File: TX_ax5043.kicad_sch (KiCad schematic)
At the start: 32 parts, among them P101 U_FL, U156 AX5043, U89 TPS22917DBV

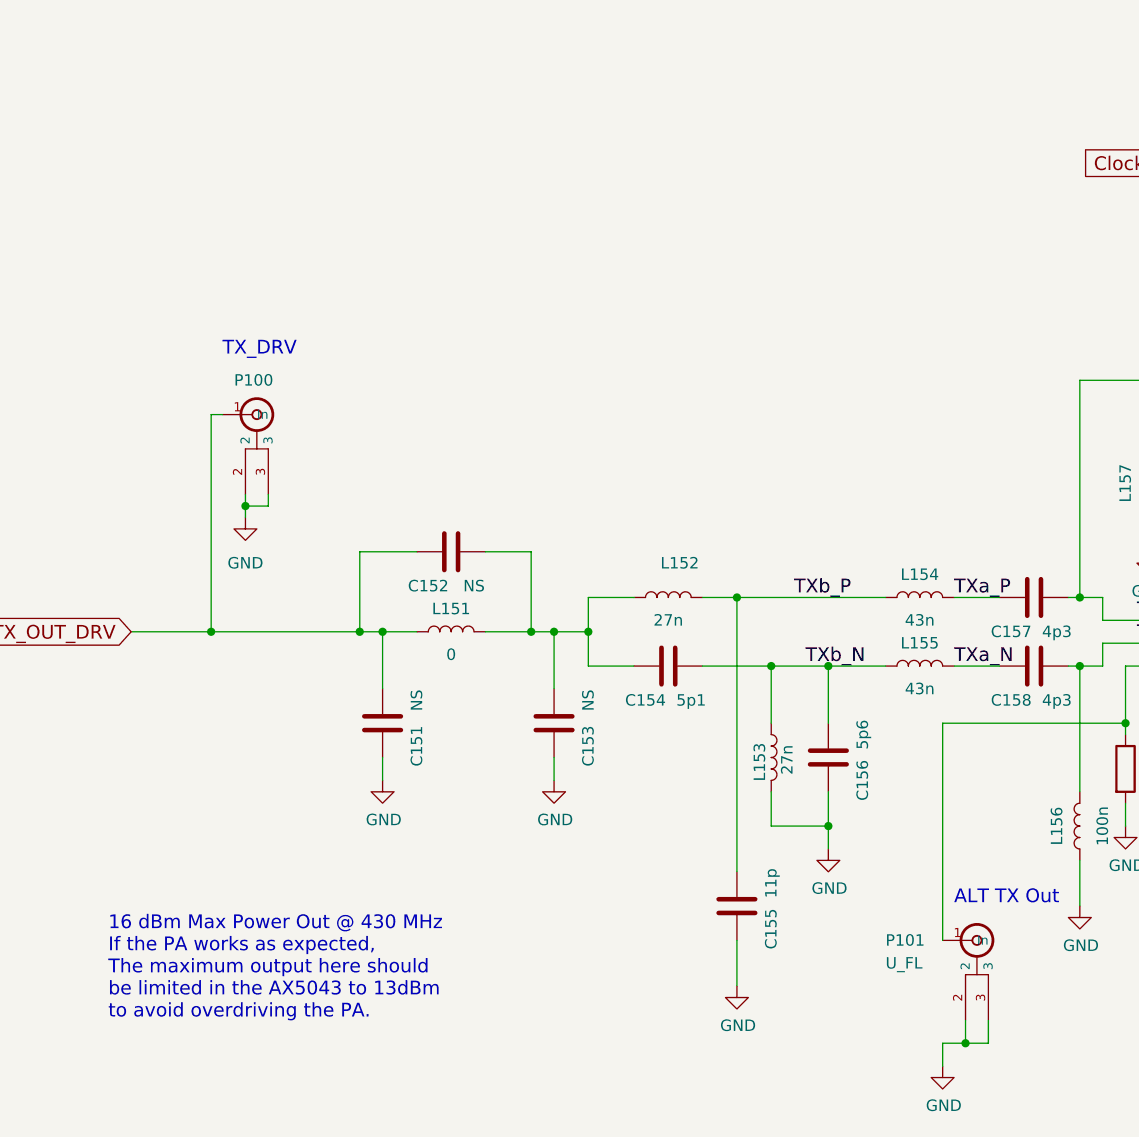
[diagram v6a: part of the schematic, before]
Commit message: Add shields around AX5043s, replace UFL connectors
Signed-off-by: Corey Minyard <corey@minyard.net>
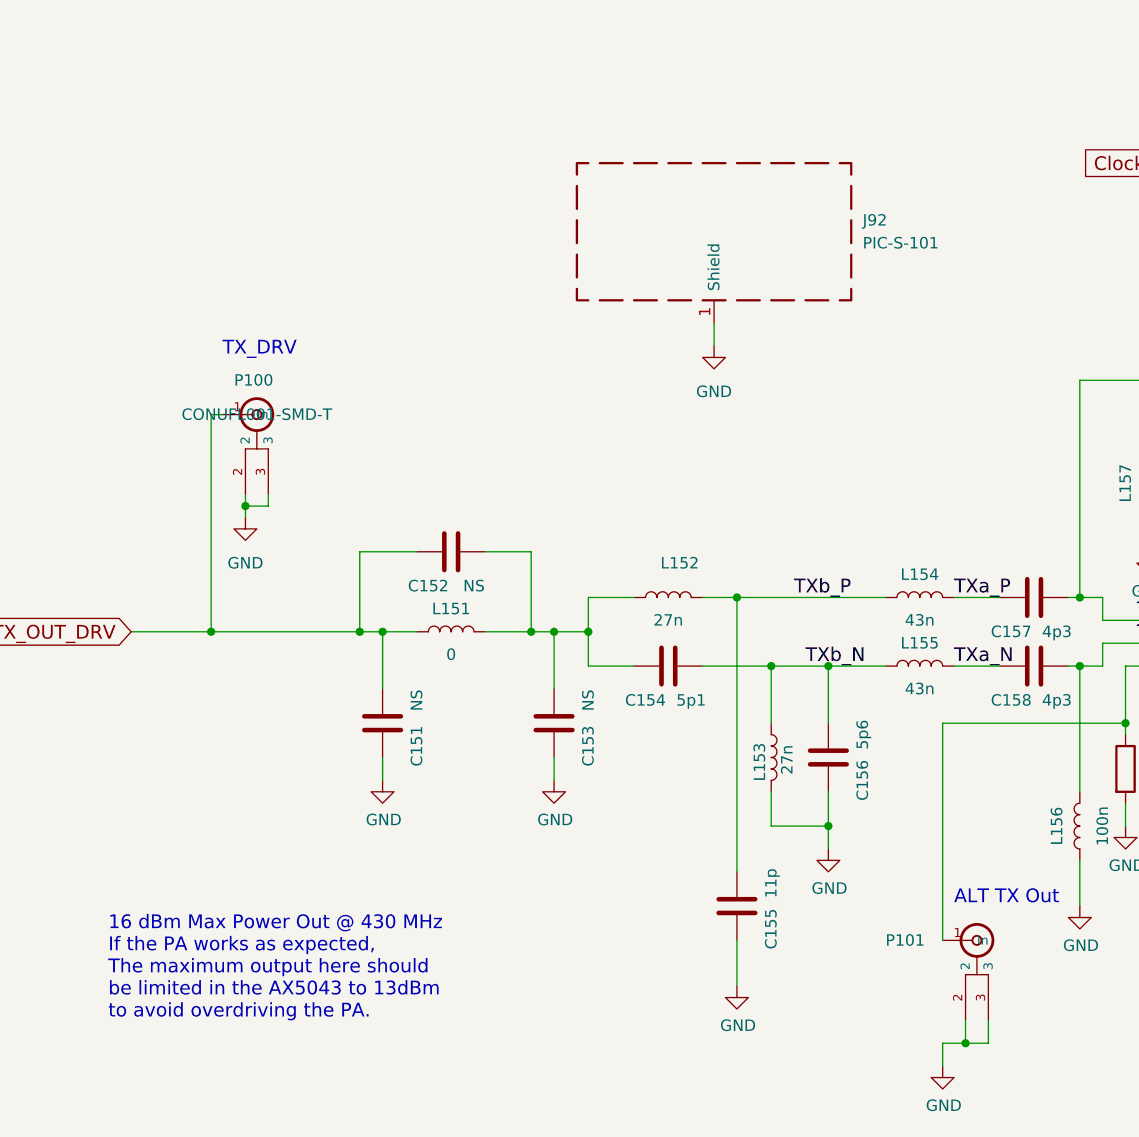
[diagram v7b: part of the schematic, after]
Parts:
- added J92: PIC-S-101, PacSatDev_misc:RF_SHIELD_PIC_S_101, symbol Device:RFShield_OnePiece
- P100: value ~ -> CONUFL001-SMD-T; footprint PacSatDev_misc:U_FL -> PacSatDev_misc:CONN1_CONUFL_TEC
- P101: value U_FL -> CONUFL001-SMD-T; footprint PacSatDev_misc:U_FL -> PacSatDev_misc:CONN1_CONUFL_TEC
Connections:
- net GND: now also J92.1 (Shield)
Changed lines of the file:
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@@
 	(wire
 		(pts
+			(xy 177.8 101.6) (xy 177.8 104.14)
+		)
+		(stroke
+			(width 0)
+			(type default)
+		)
+	)
+	(wire
+		(pts
 			(xy 256.54 176.53) (xy 262.89 176.53)
 		)
@@
 	)
 	(symbol
+		(lib_id "power:GND")
+		(at 177.8 104.14 0)
+		(unit 1)
+		(exclude_from_sim no)
+		(in_bom yes)
+		(on_board yes)
+		(dnp no)
+		(fields_autoplaced yes)
+		(property "Reference" "#PWR0208"
+			(at 177.8 110.49 0)
+			(effects
+				(font
+					(size 1.27 1.27)
+				)
+				(hide yes)
+			)
+		)
+		(property "Value" "GND"
+			(at 177.8 109.22 0)
+			(effects
+				(font
+					(size 1.27 1.27)
+				)
+			)
+		)
+		(property "Footprint" ""
+			(at 177.8 104.14 0)
+			(effects
+				(font
+					(size 1.27 1.27)
+				)
+				(hide yes)
+			)
+		)
+		(property "Datasheet" ""
+			(at 177.8 104.14 0)
+			(effects
+				(font
+					(size 1.27 1.27)
+				)
+				(hide yes)
+			)
+		)
+		(property "Description" ""
+			(at 177.8 104.14 0)
+			(effects
+				(font
+					(size 1.27 1.27)
+				)
+			)
+		)
+		(pin "1"
+		)
+		(instances
+			(project "PacSat_AFSK"
+				(path "/cc9f42d2-6985-41ac-acab-5ab7b01c5b38/00000000-0000-0000-0000-00005a014be3"
+					(reference "#PWR0208")
+					(unit 1)
+				)
+			)
+		)
+	)
+	(symbol
 		(lib_id "Device:L")
 		(at 148.59 135.89 90)
@@
 			)
 		)
-		(property "Value" "U_FL"
+		(property "Value" "CONUFL001-SMD-T"
 			(at 196.85 172.72 0)
 			(effects
@@
 				)
 				(justify left)
+				(hide yes)
 			)
 		)
-		(property "Footprint" "PacSatDev_misc:U_FL"
+		(property "Footprint" "PacSatDev_misc:CONN1_CONUFL_TEC"
 			(at 207.01 170.18 0)
 			(effects
@@
 	)
 	(symbol
+		(lib_id "Device:RFShield_OnePiece")
+		(at 177.8 91.44 0)
+		(unit 1)
+		(exclude_from_sim no)
+		(in_bom yes)
+		(on_board yes)
+		(dnp no)
+		(fields_autoplaced yes)
+		(property "Reference" "J92"
+			(at 194.31 90.1699 0)
+			(effects
+				(font
+					(size 1.27 1.27)
+				)
+				(justify left)
+			)
+		)
+		(property "Value" "PIC-S-101"
+			(at 194.31 92.7099 0)
+			(effects
+				(font
+					(size 1.27 1.27)
+				)
+				(justify left)
+			)
+		)
+		(property "Footprint" "PacSatDev_misc:RF_SHIELD_PIC_S_101"
+			(at 177.8 93.98 0)
+			(effects
+				(font
+					(size 1.27 1.27)
+				)
+				(hide yes)
+			)
+		)
+		(property "Datasheet" "~"
+			(at 177.8 93.98 0)
+			(effects
+				(font
+					(size 1.27 1.27)
+				)
+				(hide yes)
+			)
+		)
+		(property "Description" "One-piece EMI RF shielding cabinet"
+			(at 177.8 91.44 0)
+			(effects
+				(font
+					(size 1.27 1.27)
+				)
+				(hide yes)
+			)
+		)
+		(pin "1"
+		)
+		(instances
+			(project "PacSat_AFSK"
+				(path "/cc9f42d2-6985-41ac-acab-5ab7b01c5b38/00000000-0000-0000-0000-00005a014be3"
+					(reference "J92")
+					(unit 1)
+				)
+			)
+		)
+	)
+	(symbol
 		(lib_id "Device:L")
 		(at 218.44 157.48 180)
@@
 			)
 		)
-		(property "Value" "~"
+		(property "Value" "CONUFL001-SMD-T"
 			(at 127 111.76 0)
 			(effects
@@
 			)
 		)
-		(property "Footprint" "PacSatDev_misc:U_FL"
+		(property "Footprint" "PacSatDev_misc:CONN1_CONUFL_TEC"
 			(at 127 111.76 0)
 			(effects

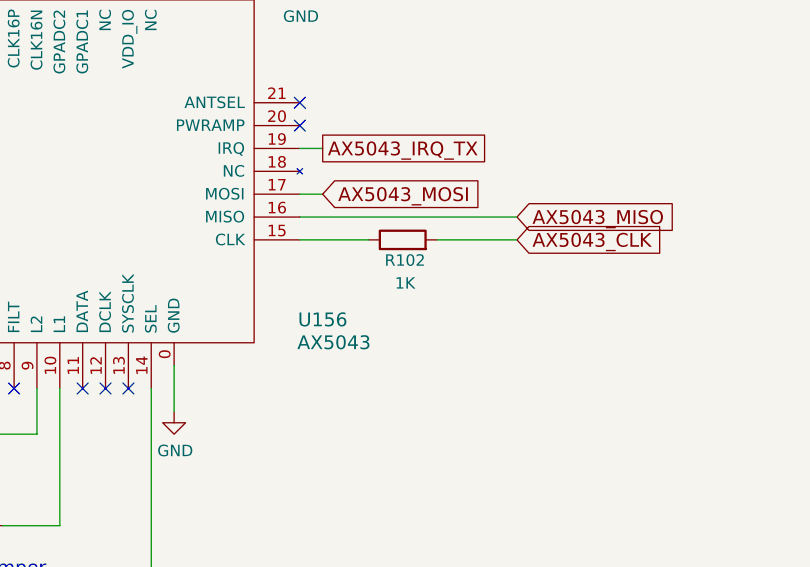
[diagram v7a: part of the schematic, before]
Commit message: Update SPI clock with simulation
Simulated the SPI clocks, updated resistor values based on findings.

Signed-off-by: Corey Minyard <corey@minyard.net>
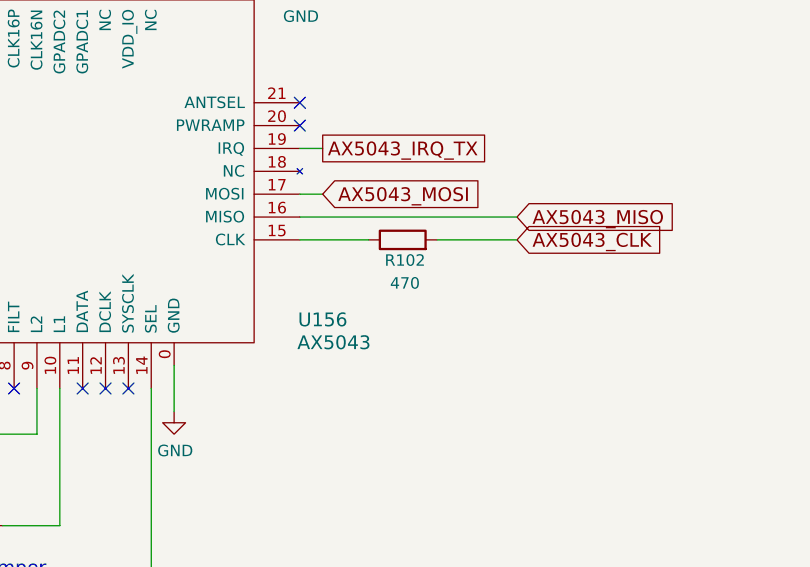
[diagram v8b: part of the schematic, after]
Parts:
- R102: value 1K -> 470
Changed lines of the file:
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@@
 			)
 		)
-		(property "Value" "1K"
+		(property "Value" "470"
 			(at 301.244 149.606 90)
 			(effects
